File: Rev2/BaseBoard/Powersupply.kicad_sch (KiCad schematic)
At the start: 13 parts, among them J1 Conn_01x02_Socket, U1 AMS1117-3.3, U2 AMS1117-5.0

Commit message: Added Testpoints, UART and JTAG
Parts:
- added TP1, TP11, TP12, TP2, TP3: TestPoint, symbol Connector:TestPoint
- J1: value Conn_01x02_Socket -> 230V CON; footprint (none) -> Connector_PinSocket_2.54mm:PinSocket_1x02_P2.54mm_Vertical
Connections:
- net +3.3V: now also TP2.1
- net +5V: now also TP3.1
- net GND: now also TP12.1
- net GND_LED: now also TP11.1
- net at C1.1, D2.1 (K), D4.1 (K)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: now also TP1.1

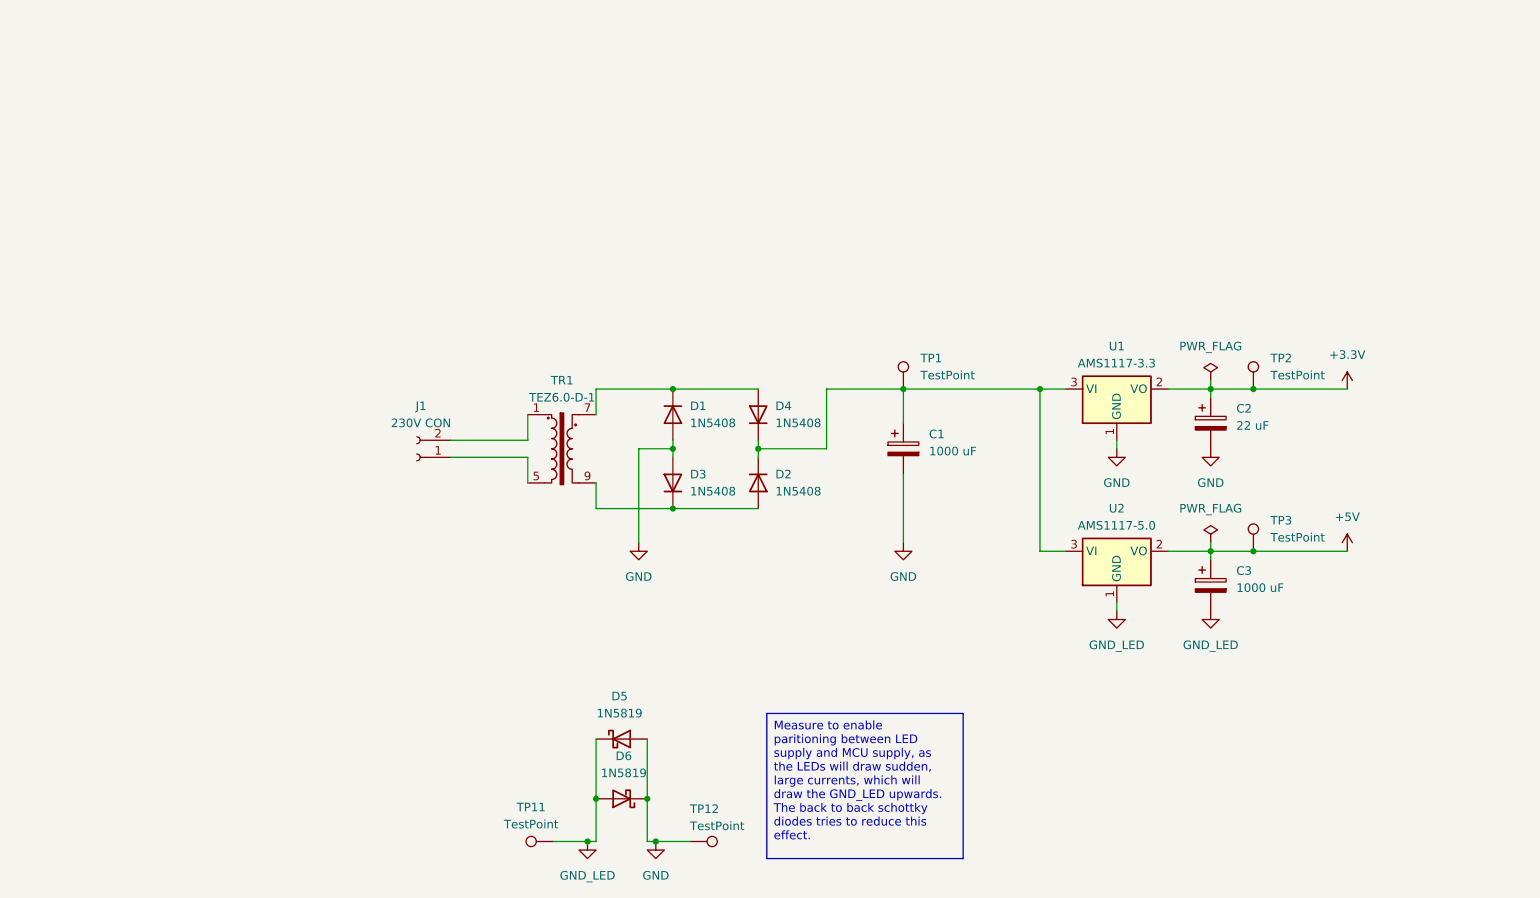
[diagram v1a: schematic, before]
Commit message: Finished placement, routing remains
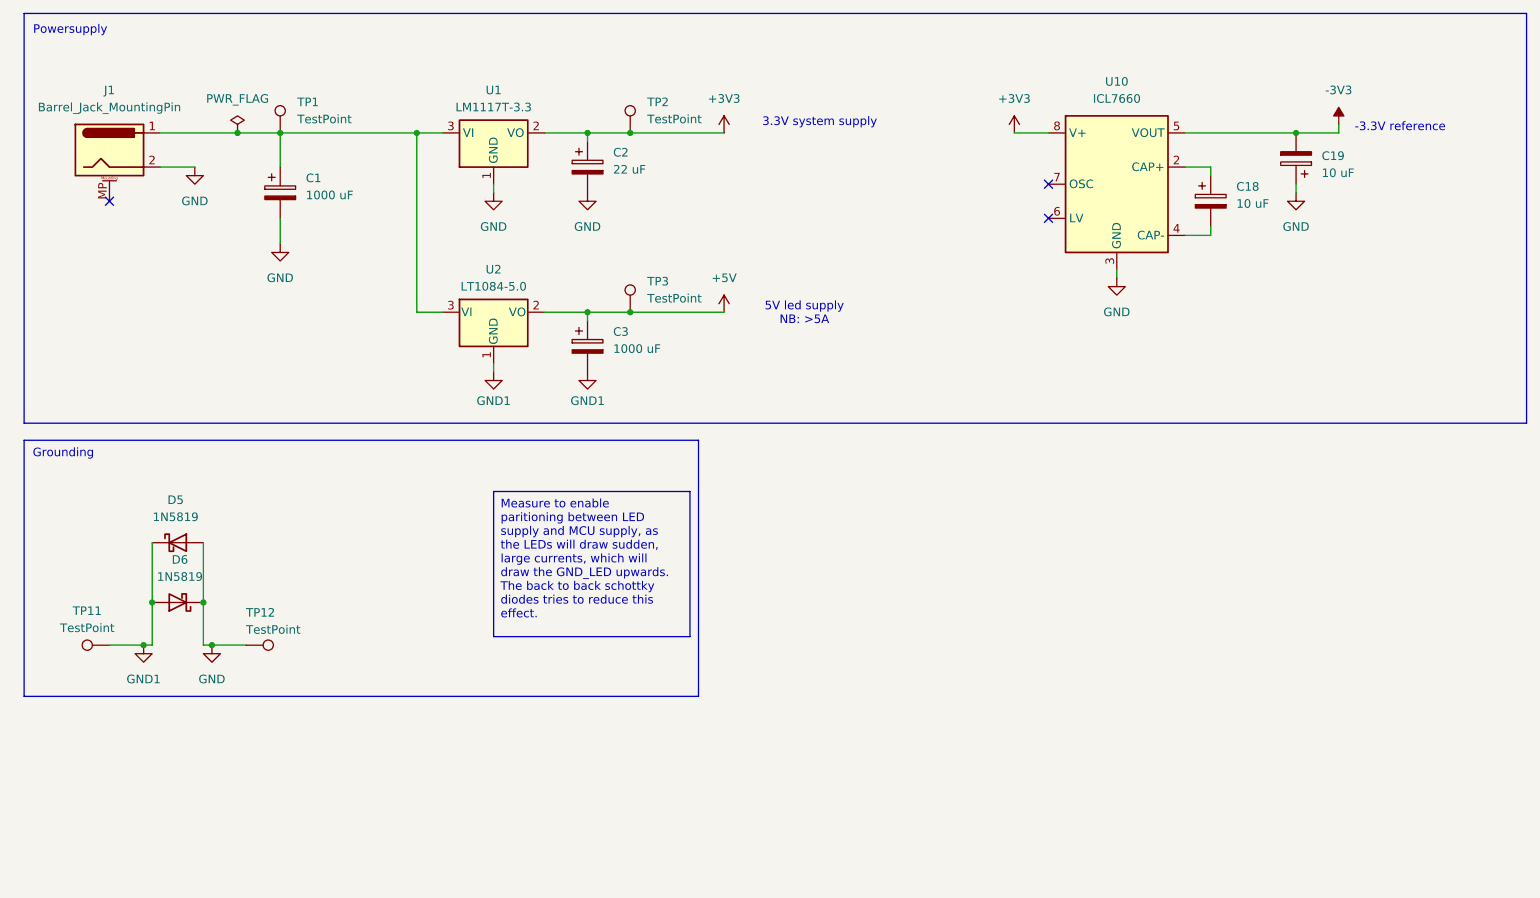
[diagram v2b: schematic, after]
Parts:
- removed D1, D2, D3, D4: 1N5408, Diode_THT:D_DO-201AD_P15.24mm_Horizontal, symbol Diode:1N5408
- removed J1: 230V CON, Connector_PinSocket_2.54mm:PinSocket_1x02_P2.54mm_Vertical, symbol Connector:Conn_01x02_Socket
- removed TR1: TEZ6.0-D-1, Transformer_THT:Transformer_Breve_TEZ-38x45, symbol Transformer:TEZ6.0-D-1
- removed U1: AMS1117-3.3, Package_TO_SOT_SMD:SOT-223-3_TabPin2, symbol Regulator_Linear:AMS1117-3.3
- removed U2: AMS1117-5.0, Package_TO_SOT_SMD:SOT-223-3_TabPin2, symbol Regulator_Linear:AMS1117-5.0
- added C18, C19: 10 uF, Capacitor_THT:CP_Radial_D4.0mm_P2.00mm, symbol Device:C_Polarized
- added J1: Barrel_Jack_MountingPin, Connector_BarrelJack:BarrelJack_Wuerth_694108106102_2.5x5.5mm, symbol Connector:Barrel_Jack_MountingPin
- added U1: LM1117T-3.3, Package_TO_SOT_THT:TO-220-3_Vertical, symbol Regulator_Linear:LM1117T-3.3
- added U10: ICL7660, USR_LIB:ICL7660, symbol Regulator_SwitchedCapacitor:ICL7660
- added U2: LT1084-5.0, Package_TO_SOT_THT:TO-220-3_Vertical, symbol Regulator_Linear:LT1084-5.0
- C1, C3: footprint (none) -> Capacitor_THT:CP_Radial_D10.0mm_P7.50mm
- C2: footprint (none) -> Capacitor_THT:CP_Radial_D6.3mm_P2.50mm
- TP1, TP11, TP12, TP2, TP3: footprint (none) -> TestPoint:TestPoint_Pad_1.0x1.0mm
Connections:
- net +5V: now also U2.2 (VO)
- net GND: now also C19.1, J1.2, U1.1 (GND), U10.3 (GND)
- net at C1.1, TP1.1: now also J1.1, U1.3 (VI), U2.3 (VI)
- net +3.3V renamed +3V3
- net +3V3: now also U1.2 (VO), U10.8 (V+)
- net GND_LED renamed GND1
- net GND1: now also U2.1 (GND)
- new net: C18.1, U10.2 (CAP+)
- new net: C18.2, U10.4 (CAP-)
- new net -3V3: C19.2, U10.5 (VOUT)
- no-connect marks 0 -> 3
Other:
- note added: "-3.3V reference"
- note added: "3.3V system supply"
- note added: "5V led supply NB: >5A"
- note added: "Grounding"
- note added: "Powersupply"
- moved on the sheet: C1, C2, C3, D5, D6, TP1, TP11, TP12, TP2, TP3
